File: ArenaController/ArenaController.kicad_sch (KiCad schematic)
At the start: 33 parts, among them J1 RJ45, J2 RJ45, J4 RJ45, J5 RJ45, J6 RJ45, J7 Barrel_Jack, J8 Screw_Terminal_01x04, Q1 FS3400, Q2 FS3400, Q3 FS3400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

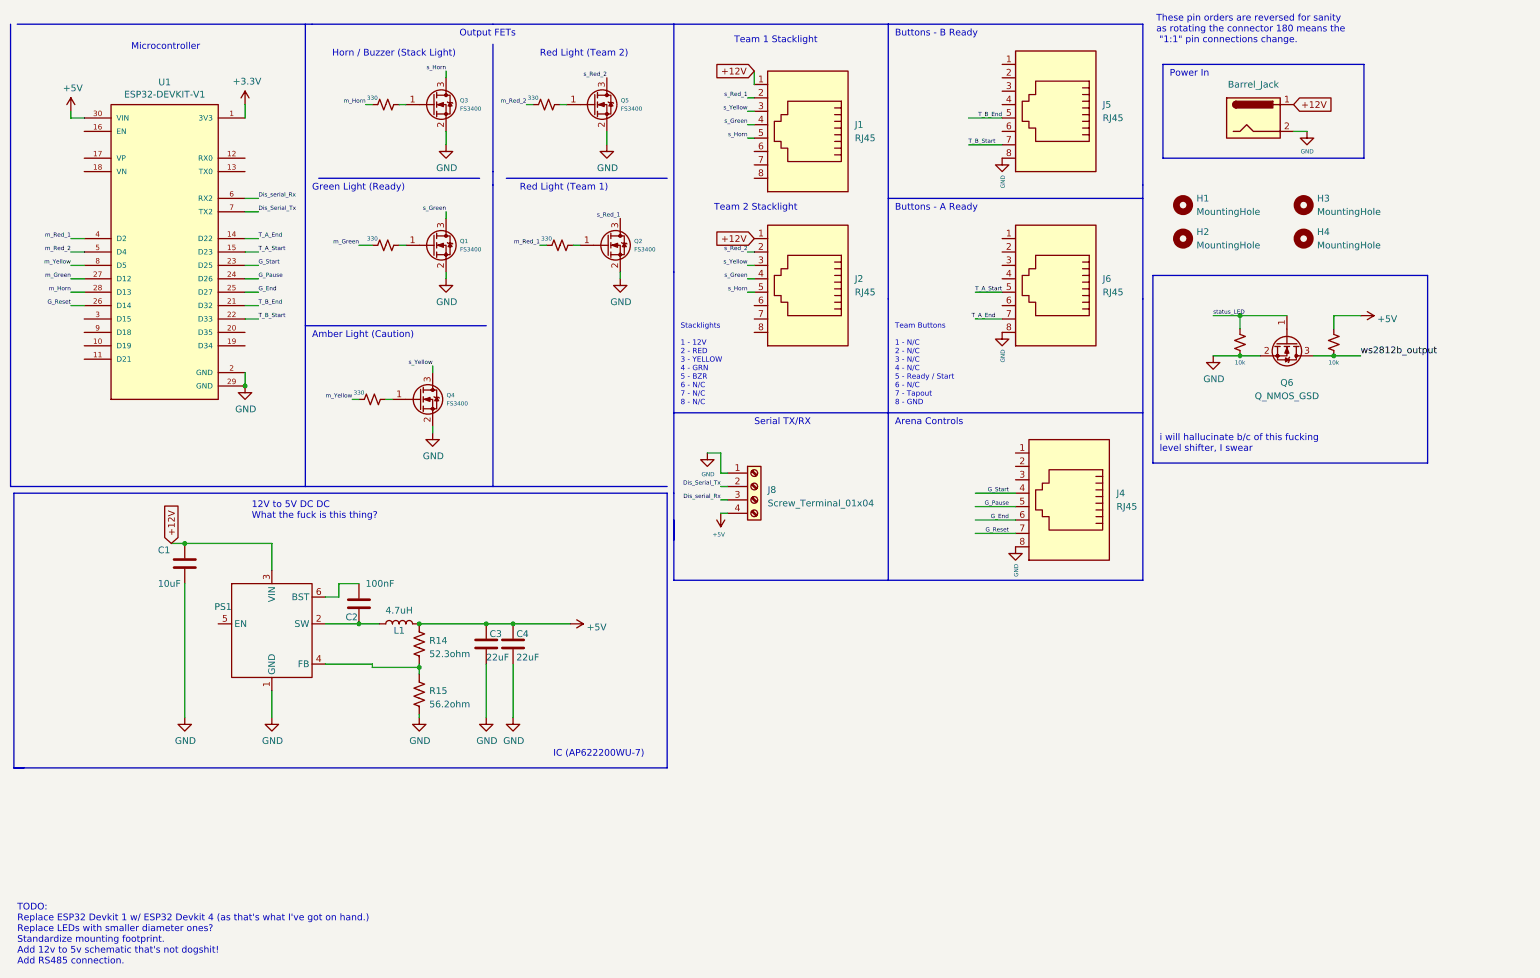
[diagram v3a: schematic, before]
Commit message: Added new DC DC symbol.
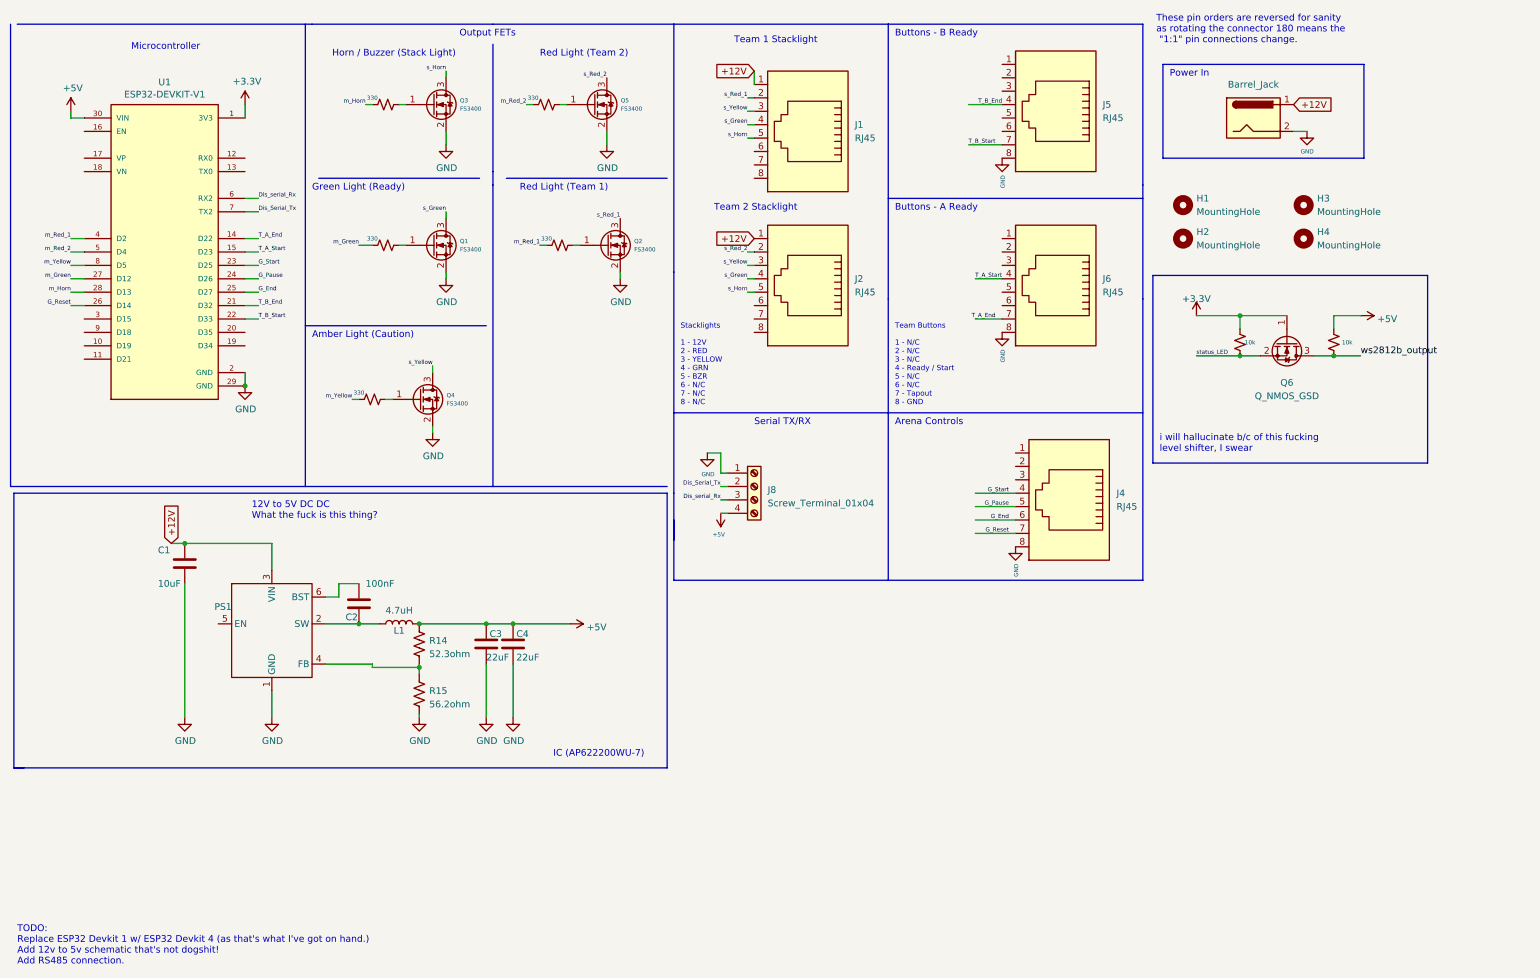
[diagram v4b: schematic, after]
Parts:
- Q6: footprint (none) -> Package_TO_SOT_SMD:SOT-23
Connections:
- net GND: no longer Q6.2 (S), R16.2
- net T_A_Start: now also J6.4; no longer J6.5
- net T_B_End: now also J5.4; no longer J5.5
- net status_LED: now also Q6.2 (S), R16.2; no longer Q6.1 (G), R16.1
- new net +3.3V: Q6.1 (G), R16.1
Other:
- note added: "TODO: Replace ESP32 Devkit 1 w/ ESP32 Devkit 4 (as that's what I've got on hand.) Add 12v to 5v schematic that's not dogshit! Add RS485 connection."
- note added: "Team Buttons 1 - N/C 2 - N/C 3 - N/C 4 - Ready / Start 5 - N/C 6 - N/C 7 - Tapout 8 - GND"
- note removed: "TODO: Replace ESP32 Devkit 1 w/ ESP32 Devkit 4 (as that's what I've got on hand.) Replace LEDs with smaller diameter ones? Standardize mounting footprint. Add 12v to 5v schematic that's not dogshit! Add RS485 connection."
- note removed: "Team Buttons 1 - N/C 2 - N/C 3 - N/C 4 - N/C 5 - Ready / Start 6 - N/C 7 - Tapout 8 - GND"
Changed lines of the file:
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@@
     (stroke (width 0) (type default))
   )
-  (wire (pts (xy 198.12 67.31) (xy 203.2 67.31))
+  (wire (pts (xy 198.12 64.77) (xy 203.2 64.77))
     (stroke (width 0) (type default))
   )
@@
     (stroke (width 0) (type default))
   )
-  (wire (pts (xy 243.205 79.375) (xy 248.285 79.375))
+  (wire (pts (xy 240.03 79.375) (xy 248.285 79.375))
     (stroke (width 0) (type default))
   )
@@
     (stroke (width 0) (type default))
   )
-  (wire (pts (xy 243.205 71.755) (xy 248.285 71.755))
+  (wire (pts (xy 240.03 71.755) (xy 248.285 71.755))
     (stroke (width 0) (type default))
   )
@@
     (stroke (width 0) (type default))
   )
-  (wire (pts (xy 196.85 34.29) (xy 203.2 34.29))
+  (wire (pts (xy 196.85 31.75) (xy 203.2 31.75))
     (stroke (width 0) (type default))
   )
@@
     (effects (font (size 1.27 1.27)) (justify left bottom))
   )
-  (text "TODO:\nReplace ESP32 Devkit 1 w/ ESP32 Devkit 4 (as that's what I've got on hand.)\nReplace LEDs with smaller diameter ones?\nStandardize mounting footprint.\nAdd 12v to 5v schematic that's not dogshit!\nAdd RS485 connection."
+  (text "TODO:\nReplace ESP32 Devkit 1 w/ ESP32 Devkit 4 (as that's what I've got on hand.)\nAdd 12v to 5v schematic that's not dogshit!\nAdd RS485 connection."
     (at 16.51 194.945 0)
     (effects (font (size 1.27 1.27)) (justify left bottom))
@@
     (effects (font (size 1.27 1.27)) (justify left bottom))
   )
-  (text "Team Buttons\n\n1 - N/C\n2 - N/C\n3 - N/C\n4 - N/C\n5 - Ready / Start\n6 - N/C\n7 - Tapout\n8 - GND"
+  (text "Team Buttons\n\n1 - N/C\n2 - N/C\n3 - N/C\n4 - Ready / Start\n5 - N/C\n6 - N/C\n7 - Tapout\n8 - GND"
     (at 182.88 88.9 0)
     (effects (font (size 1 1)) (justify left bottom))
@@
     (effects (font (size 0.7874 0.7874)) (justify right bottom))
   )
-  (label "T_B_End" (at 203.2 34.29 180) (fields_autoplaced)
+  (label "T_B_End" (at 203.2 31.75 180) (fields_autoplaced)
     (effects (font (size 0.7874 0.7874)) (justify right bottom))
   )
@@
     (effects (font (size 0.7874 0.7874)) (justify left bottom))
   )
-  (label "T_A_Start" (at 203.2 67.31 180) (fields_autoplaced)
+  (label "T_A_Start" (at 203.2 64.77 180) (fields_autoplaced)
     (effects (font (size 0.7874 0.7874)) (justify right bottom))
   )
@@
     (effects (font (size 0.7874 0.7874)) (justify right bottom))
   )
-  (label "status_LED" (at 243.205 71.755 0) (fields_autoplaced)
+  (label "status_LED" (at 240.03 79.375 0) (fields_autoplaced)
     (effects (font (size 0.7874 0.7874)) (justify left bottom))
   )
@@
       (effects (font (size 1.27 1.27)) hide)
     )
-    (property "Value" "10k" (at 248.285 80.645 0)
+    (property "Value" "10k" (at 250.19 76.835 0)
       (effects (font (size 0.7874 0.7874)))
     )
@@
         (path "/156576da-4c7a-4c71-af43-7540e3a24bd3"
           (reference "C2") (unit 1)
-        )
-      )
-    )
-  )
-  (symbol (lib_id "power:GND") (at 243.205 79.375 0) (unit 1)
-    (in_bom yes) (on_board yes) (dnp no)
-    (property "Reference" "#PWR0120" (at 243.205 85.725 0)
-      (effects (font (size 1.27 1.27)) hide)
-    )
-    (property "Value" "GND" (at 243.332 83.7692 0)
-      (effects (font (size 1.27 1.27)))
-    )
-    (property "Footprint" "" (at 243.205 79.375 0)
-      (effects (font (size 1.27 1.27)) hide)
-    )
-    (property "Datasheet" "" (at 243.205 79.375 0)
-      (effects (font (size 1.27 1.27)) hide)
-    )
-    (pin "1")
-    (instances
-      (project "ArenaController"
-        (path "/156576da-4c7a-4c71-af43-7540e3a24bd3"
-          (reference "#PWR0120") (unit 1)
         )
       )
@@
     )
   )
+  (symbol (lib_id "power:+3.3V") (at 240.03 71.755 0) (unit 1)
+    (in_bom yes) (on_board yes) (dnp no) (fields_autoplaced)
+    (property "Reference" "#PWR03" (at 240.03 75.565 0)
+      (effects (font (size 1.27 1.27)) hide)
+    )
+    (property "Value" "+3.3V" (at 240.03 68.58 0)
+      (effects (font (size 1.27 1.27)))
+    )
+    (property "Footprint" "" (at 240.03 71.755 0)
+      (effects (font (size 1.27 1.27)) hide)
+    )
+    (property "Datasheet" "" (at 240.03 71.755 0)
+      (effects (font (size 1.27 1.27)) hide)
+    )
+    (pin "1")
+    (instances
+      (project "ArenaController"
+        (path "/156576da-4c7a-4c71-af43-7540e3a24bd3"
+          (reference "#PWR03") (unit 1)
+        )
+      )
+    )
+  )
   (symbol (lib_id "Device:Q_NMOS_GSD") (at 257.175 76.835 270) (unit 1)
     (in_bom yes) (on_board yes) (dnp no) (fields_autoplaced)
@@
       (effects (font (size 1.27 1.27)))
     )
-    (property "Footprint" "" (at 259.715 81.915 0)
+    (property "Footprint" "Package_TO_SOT_SMD:SOT-23" (at 259.715 81.915 0)
       (effects (font (size 1.27 1.27)) hide)
     )
@@
       (effects (font (size 1.27 1.27)) hide)
     )
-    (property "Value" "10k" (at 266.065 80.645 0)
+    (property "Value" "10k" (at 268.605 76.835 0)
       (effects (font (size 0.7874 0.7874)))
     )

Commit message: Added more SMD nightmare parts.
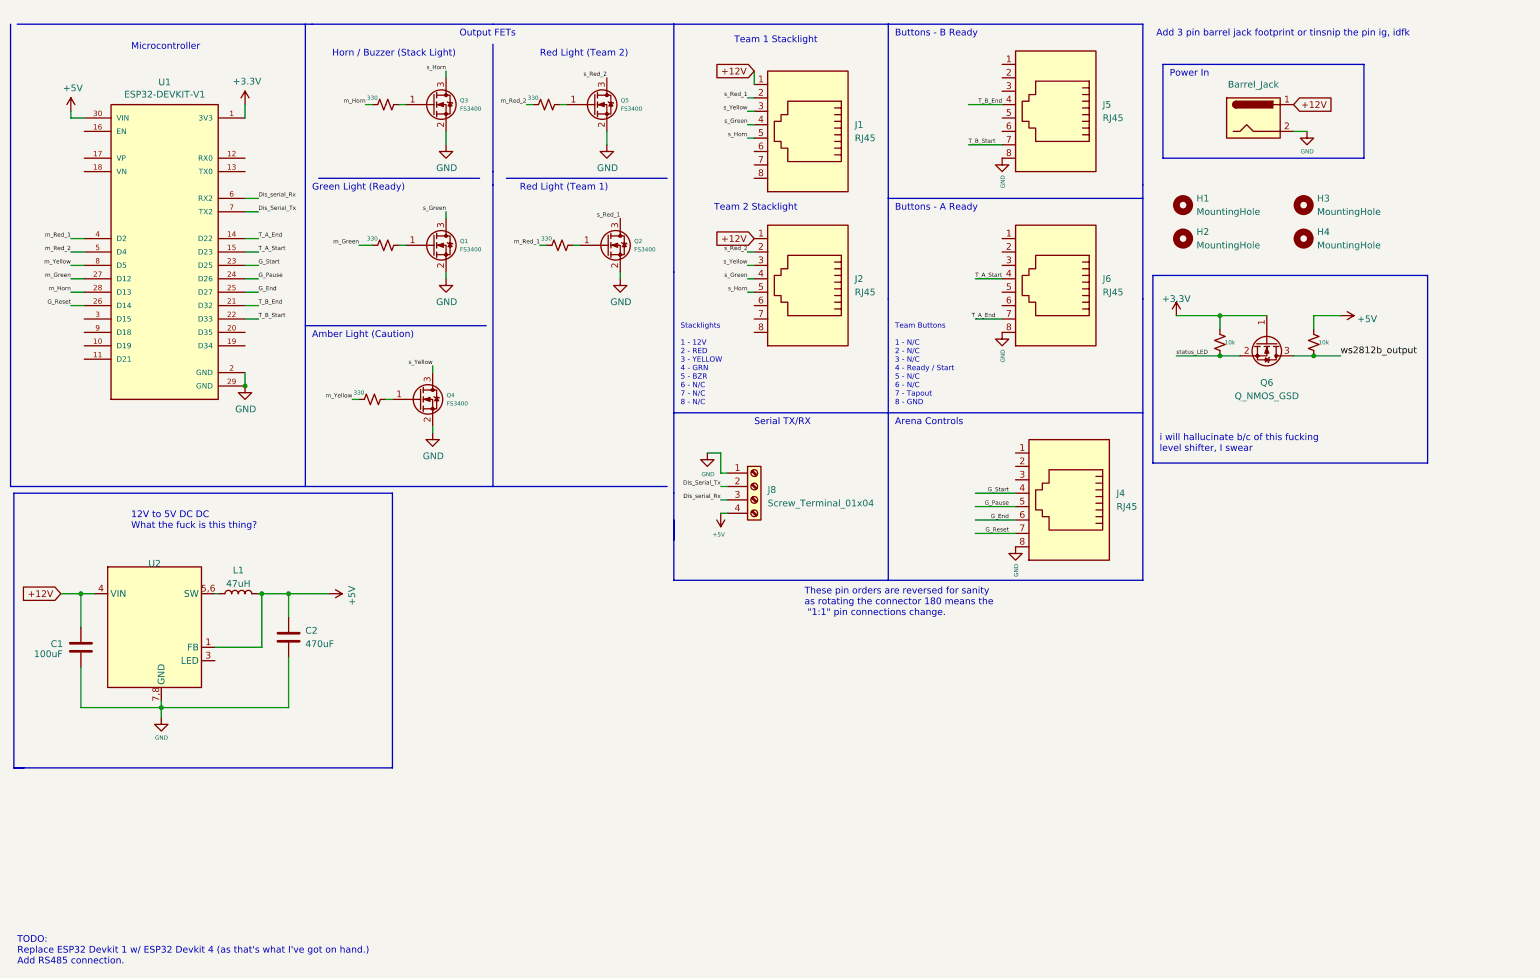
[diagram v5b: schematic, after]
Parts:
- removed C3, C4: 22uF, symbol Device:C
- removed PS1: ~, Package_TO_SOT_SMD:TSOT-23-6_HandSoldering, symbol symbols:AP62200
- removed R14: 52.3ohm, symbol Device:R_US
- removed R15: 56.2ohm, symbol Device:R_US
- removed R17: 10k, Resistor_THT:R_Axial_DIN0207_L6.3mm_D2.5mm_P10.16mm_Horizontal, symbol Device:R_Small_US
- removed R6: 330, Resistor_THT:R_Axial_DIN0207_L6.3mm_D2.5mm_P10.16mm_Horizontal, symbol Device:R_Small_US
- added R1: 330, Resistor_SMD:R_0603_1608Metric_Pad0.98x0.95mm_HandSolder, symbol Device:R_Small_US
- added R7: 10k, Resistor_SMD:R_0603_1608Metric_Pad0.98x0.95mm_HandSolder, symbol Device:R_Small_US
- added U2: ~, Package_SO:SOP-8_3.76x4.96mm_P1.27mm, symbol symbols:TX4140
- C1: value 10uF -> 100uF; footprint (none) -> Capacitor_SMD:C_Elec_6.3x5.4; LCSC (none) -> https://www.lcsc.com/product-detail/Aluminum-Electrolytic-C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
- C2: value 100nF -> 470uF; footprint (none) -> Capacitor_SMD:C_Elec_6.3x7.7; LCSC (none) -> https://www.lcsc.com/product-detail/Aluminum-Electrolytic-C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
- J7: LCSC (none) -> https://www.lcsc.com/product-detail/AC-DC-Power-Connectors_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
- J8: footprint TerminalBlock_MetzConnect:TerminalBlock_MetzConnect_Type011_RT05504HBWC_1x04_P5.00mm_Horizontal -> Connector_PinSocket_2.54mm:PinSocket_1x04_P2.54mm_Vertical
- L1: value 4.7uH -> 47uH; footprint (none) -> Inductor_SMD:L_0603_1608Metric; LCSC (none) -> https://www.lcsc.com/product-detail/Inductors-SMD_PROD-Tech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
- R16, R2, R3, R4, R5: footprint Resistor_THT:R_Axial_DIN0207_L6.3mm_D2.5mm_P10.16mm_Horizontal -> Resistor_SMD:R_0603_1608Metric_Pad0.98x0.95mm_HandSolder; LCSC (none) -> https://www.lcsc.com/product-detail/Chip-Resistor-Surface-M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
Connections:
- net +12V: now also U2.4 (VIN)
- net +5V: now also C2.2, R7.1, U2.1 (FB)
- net GND: now also C2.1, U2.7,8 (GND)
- net m_Green: now also R1.2; no longer R2.2
- net m_Horn: now also R2.2; no longer R4.2
- net m_Red_1: now also R4.2; no longer R3.2
- net m_Red_2: now also R3.2
- net ws2812b_output: now also R7.2
- net at Q2.1 (G): now also R4.1; no longer R3.1
- net at Q1.1 (G): now also R1.1; no longer R2.1
- net at Q3.1 (G): now also R2.1; no longer R4.1
- net at Q5.1 (G): now also R3.1
- net at L1.1: now also U2.5,6 (SW); no longer C2.1
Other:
- note added: "Add 3 pin barrel jack footprint or tinsnip the pin ig, idfk"
- note added: "TODO: Replace ESP32 Devkit 1 w/ ESP32 Devkit 4 (as that's what I've got on hand.) Add RS485 connection."
- note removed: "IC (AP622200WU-7)"
- note removed: "TODO: Replace ESP32 Devkit 1 w/ ESP32 Devkit 4 (as that's what I've got on hand.) Add 12v to 5v schematic that's not dogshit! Add RS485 connection."
- moved on the sheet: Q6

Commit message: Swapped to ESP32 Devkit 4.
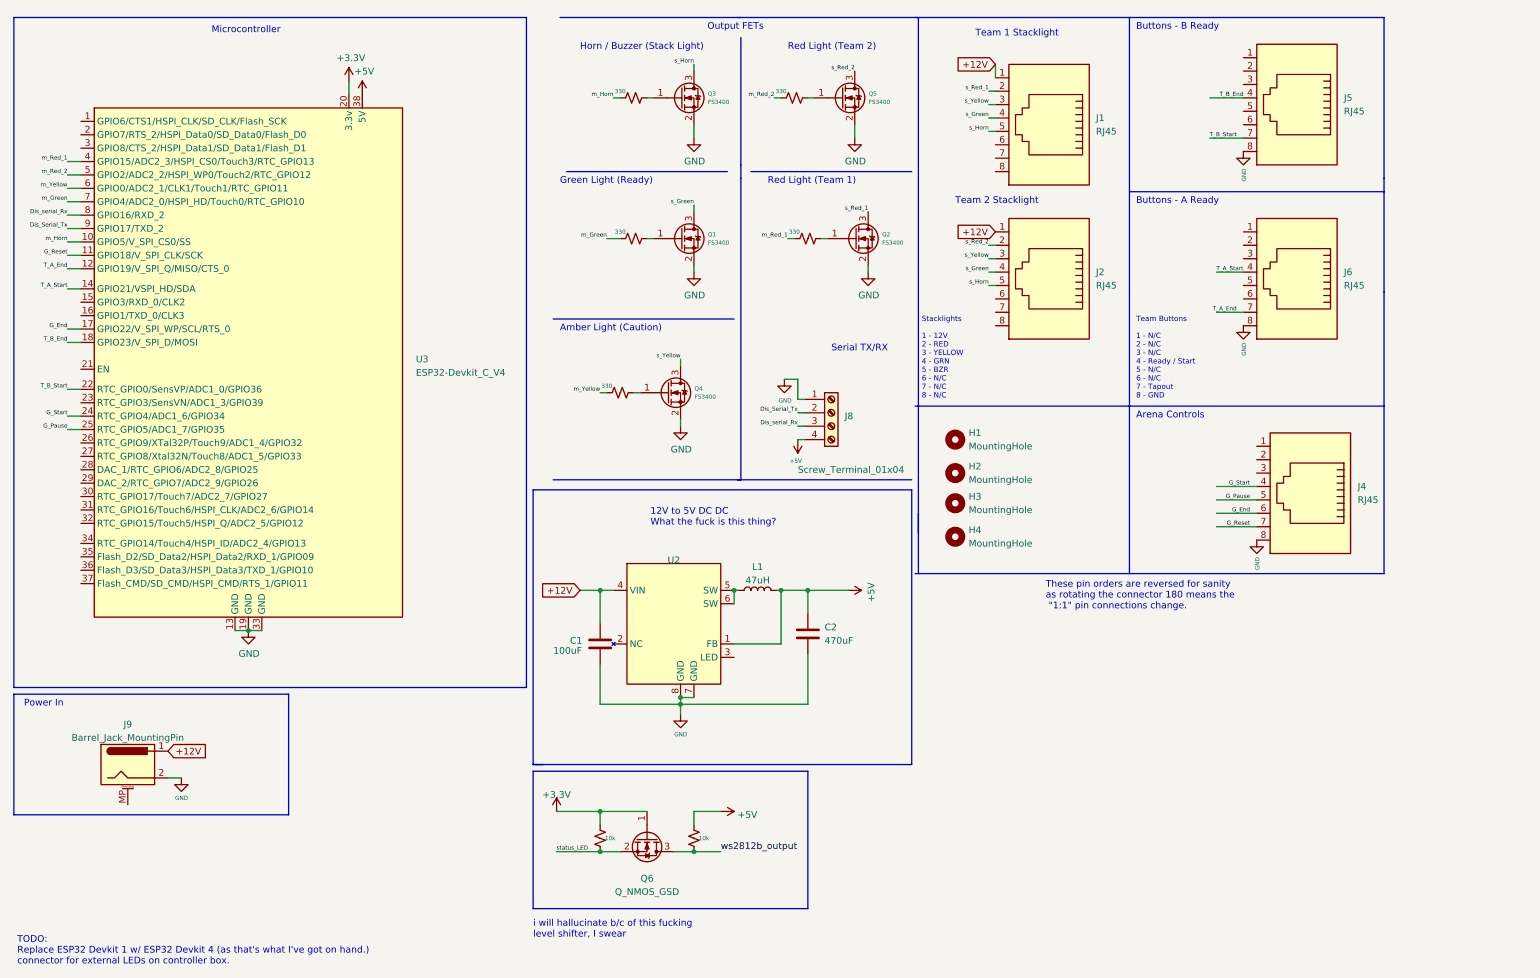
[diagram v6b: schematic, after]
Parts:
- removed J7: Barrel_Jack, footprints:BarrelJack_Horizontal_TwoPin, symbol Connector:Barrel_Jack
- removed U1: ESP32-DEVKIT-V1, ESP32DK1:MODULE_ESP32_DEVKIT_V1, symbol ESP32DK1:ESP32-DEVKIT-V1
- added J9: Barrel_Jack_MountingPin, Connector_BarrelJack:BarrelJack_Horizontal, symbol Connector:Barrel_Jack_MountingPin
- added U3: ESP32-Devkit_C_V4, footprints:MODULE_ESP32_DEVKIT_C_V4, symbol symbols:ESP32-Devkit_C_V4
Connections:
- net +12V: now also J9.1
- net +3V3: now also U3.20 (3.3v)
- net +5V: now also U3.38 (5V)
- net Dis_Serial_Tx: now also U3.9 (GPIO17/TXD_2)
- net Dis_serial_Rx: now also U3.8 (GPIO16/RXD_2)
- net GND: now also U2.7 (GND), U2.8 (GND), J9.2, U3.13 (GND), U3.19 (GND), U3.33 (GND); no longer U2.7,8 (GND)
- net G_End: now also U3.17 (GPIO22/V_SPI_WP/SCL/RTS_0)
- net G_Pause: now also U3.25 (RTC_GPIO5/ADC1_7/GPIO35)
- net G_Reset: now also U3.11 (GPIO18/V_SPI_CLK/SCK)
- net G_Start: now also U3.24 (RTC_GPIO4/ADC1_6/GPIO34)
- net T_A_End: now also U3.12 (GPIO19/V_SPI_Q/MISO/CTS_0)
- net T_A_Start: now also U3.14 (GPIO21/VSPI_HD/SDA)
- net T_B_End: now also U3.18 (GPIO23/V_SPI_D/MOSI)
- net T_B_Start: now also U3.22 (RTC_GPIO0/SensVP/ADC1_0/GPIO36)
- net m_Green: now also U3.7 (GPIO4/ADC2_0/HSPI_HD/Touch0/RTC_GPIO10)
- net m_Horn: now also U3.10 (GPIO5/V_SPI_CS0/SS)
- net m_Red_1: now also U3.4 (GPIO15/ADC2_3/HSPI_CS0/Touch3/RTC_GPIO13)
- net m_Red_2: now also U3.5 (GPIO2/ADC2_2/HSPI_WP0/Touch2/RTC_GPIO12)
- net m_Yellow: now also U3.6 (GPIO0/ADC2_1/CLK1/Touch1/RTC_GPIO11)
- net at L1.1: now also U2.5 (SW), U2.6 (SW); no longer U2.5,6 (SW)
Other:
- note added: "TODO: Replace ESP32 Devkit 1 w/ ESP32 Devkit 4 (as that's what I've got on hand.) connector for external LEDs on controller box."
- note removed: "Add 3 pin barrel jack footprint or tinsnip the pin ig, idfk"
- note removed: "TODO: Replace ESP32 Devkit 1 w/ ESP32 Devkit 4 (as that's what I've got on hand.) Add RS485 connection."
- moved on the sheet: C1, C2, H1, H2, H3, H4, J1, J2, J4, J5, J6, J8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
